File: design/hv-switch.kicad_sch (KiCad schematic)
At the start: 29 parts, among them Q3 GAN080-650EBE, U7 MAX22702EASA+

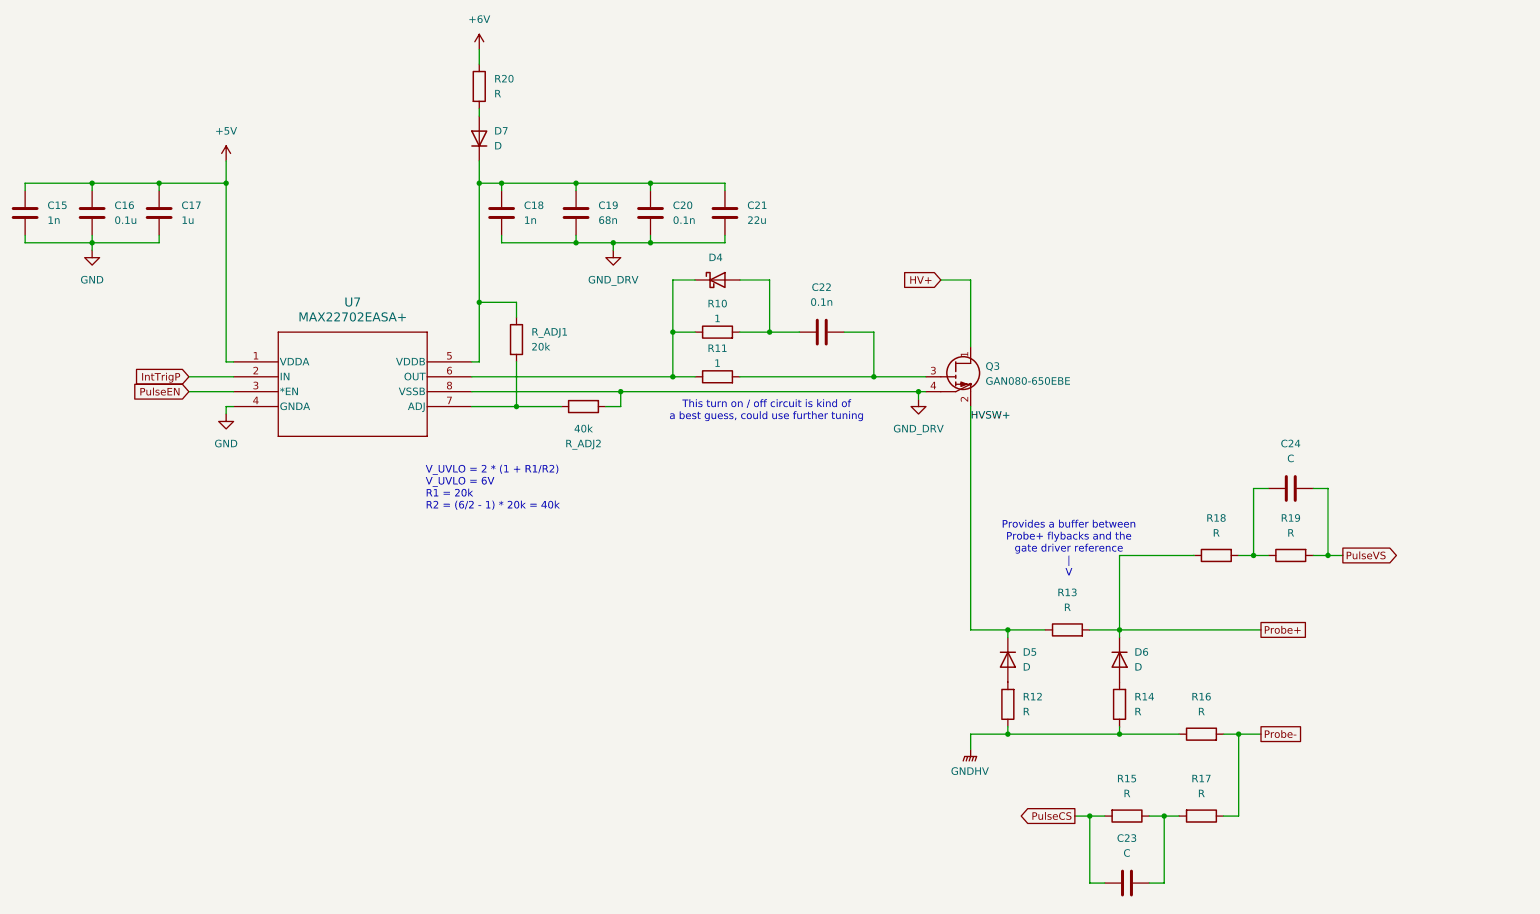
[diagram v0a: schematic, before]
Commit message: working on measurement buffers
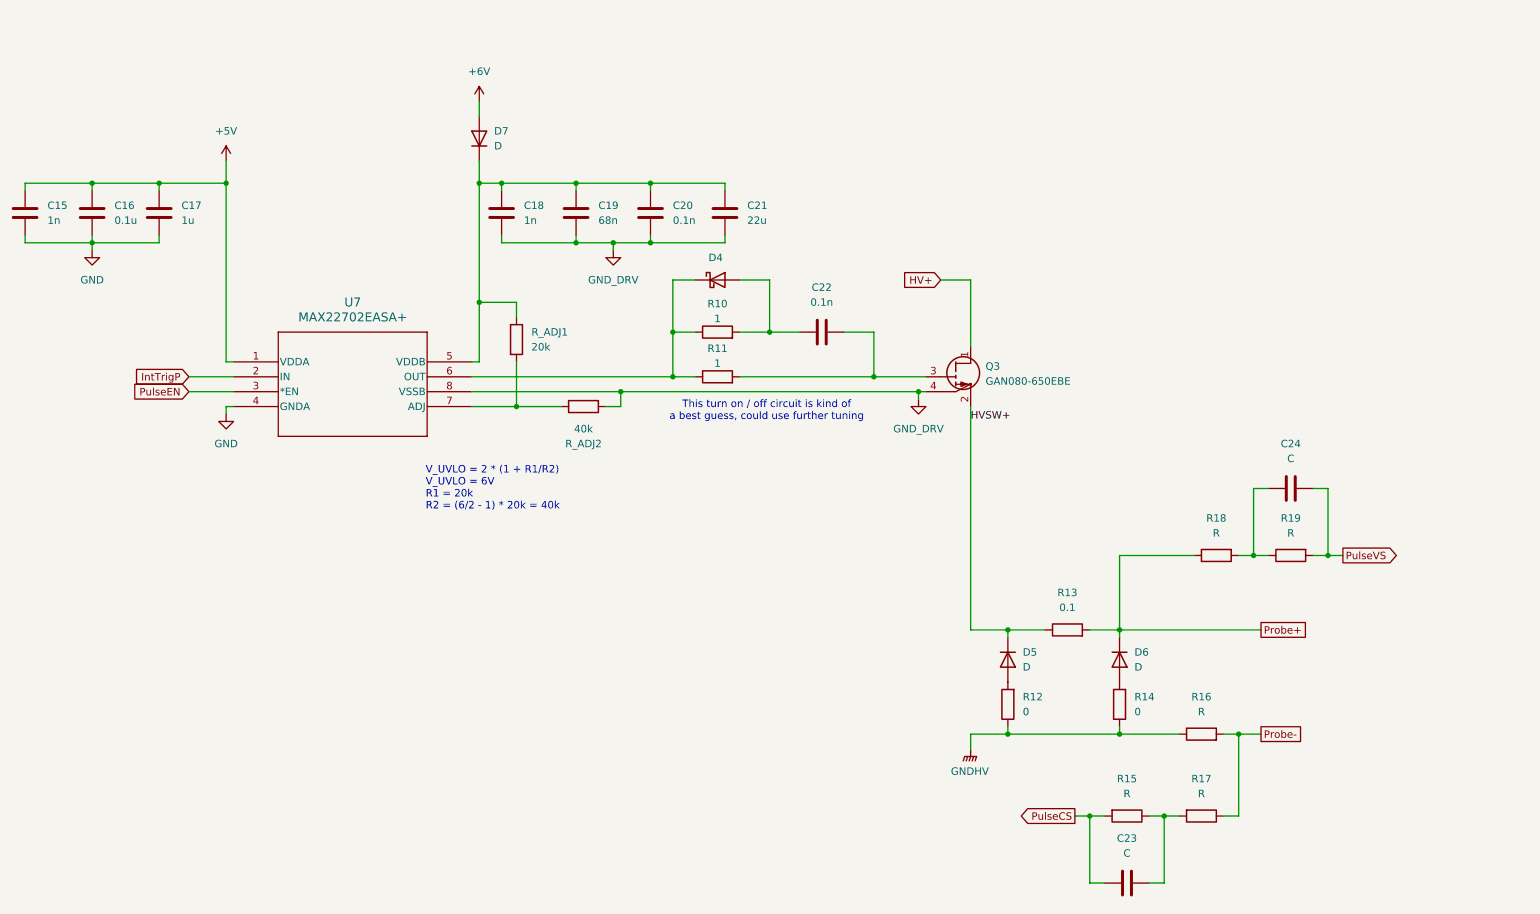
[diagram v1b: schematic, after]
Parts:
- removed R20: R, symbol Device:R
- R12, R14: value R -> 0
- R13: value R -> 0.1
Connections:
- net +6V: now also D7.2 (A)
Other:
- note removed: "Provides a buffer between Probe+ flybacks and the gate driver reference | V"
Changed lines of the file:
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@@
 		)
 	)
-	(text "Provides a buffer between \nProbe+ flybacks and the \ngate driver reference\n|\nV"
-		(exclude_from_sim no)
-		(at 212.344 105.664 0)
-		(effects
-			(font
-				(size 1.27 1.27)
-			)
-		)
-	)
 	(junction
 		(at 243.84 106.68)
@@
 	(wire
 		(pts
+			(xy 111.76 29.21) (xy 111.76 31.75)
+		)
+		(stroke
+			(width 0)
+			(type default)
+		)
+	)
+	(wire
+		(pts
 			(xy 213.36 151.13) (xy 215.9 151.13)
 		)
@@
 	(wire
 		(pts
-			(xy 111.76 30.48) (xy 111.76 31.75)
-		)
-		(stroke
-			(width 0)
-			(type default)
-		)
-	)
-	(wire
-		(pts
 			(xy 118.11 63.5) (xy 111.76 63.5)
 		)
@@
 	(wire
 		(pts
-			(xy 111.76 20.32) (xy 111.76 22.86)
-		)
-		(stroke
-			(width 0)
-			(type default)
-		)
-	)
-	(wire
-		(pts
 			(xy 241.3 151.13) (xy 238.76 151.13)
 		)
@@
 	(symbol
 		(lib_id "power:VDD")
-		(at 111.76 20.32 0)
+		(at 111.76 29.21 0)
 		(unit 1)
 		(exclude_from_sim no)
@@
 		(fields_autoplaced yes)
 		(property "Reference" "#PWR034"
-			(at 111.76 24.13 0)
+			(at 111.76 33.02 0)
 			(effects
 				(font
@@
 		)
 		(property "Value" "+6V"
-			(at 111.76 15.24 0)
+			(at 111.76 24.13 0)
 			(effects
 				(font
@@
 		)
 		(property "Footprint" ""
-			(at 111.76 20.32 0)
+			(at 111.76 29.21 0)
 			(effects
 				(font
@@
 		)
 		(property "Datasheet" ""
-			(at 111.76 20.32 0)
+			(at 111.76 29.21 0)
 			(effects
 				(font
@@
 		)
 		(property "Description" "Power symbol creates a global label with name \"VDD\""
-			(at 111.76 20.32 0)
+			(at 111.76 29.21 0)
 			(effects
 				(font
@@
 	)
 	(symbol
-		(lib_id "Device:R")
-		(at 111.76 26.67 0)
-		(unit 1)
-		(exclude_from_sim no)
-		(in_bom yes)
-		(on_board yes)
-		(dnp no)
-		(fields_autoplaced yes)
-		(property "Reference" "R20"
-			(at 114.3 25.3999 0)
-			(effects
-				(font
-					(size 1.27 1.27)
-				)
-				(justify left)
-			)
-		)
-		(property "Value" "R"
-			(at 114.3 27.9399 0)
-			(effects
-				(font
-					(size 1.27 1.27)
-				)
-				(justify left)
-			)
-		)
-		(property "Footprint" ""
-			(at 109.982 26.67 90)
-			(effects
-				(font
-					(size 1.27 1.27)
-				)
-				(hide yes)
-			)
-		)
-		(property "Datasheet" "~"
-			(at 111.76 26.67 0)
-			(effects
-				(font
-					(size 1.27 1.27)
-				)
-				(hide yes)
-			)
-		)
-		(property "Description" "Resistor"
-			(at 111.76 26.67 0)
-			(effects
-				(font
-					(size 1.27 1.27)
-				)
-				(hide yes)
-			)
-		)
-		(pin "2"
-		)
-		(pin "1"
-		)
-		(instances
-			(project ""
-				(path "/e1be550d-9ce6-42b1-a89a-c00b9d7586dd/a0344160-5a1e-4ade-9868-d857907b9d6d"
-					(reference "R20")
-					(unit 1)
-				)
-			)
-		)
-	)
-	(symbol
 		(lib_id "power:VDD")
 		(at 68.58 39.37 0)
@@
 			)
 		)
-		(property "Value" "R"
+		(property "Value" "0"
 			(at 204.47 133.3499 0)
 			(effects
@@
 			)
 		)
-		(property "Value" "R"
+		(property "Value" "0.1"
 			(at 212.09 115.57 90)
 			(effects
@@
 			)
 		)
-		(property "Value" "R"
+		(property "Value" "0"
 			(at 223.52 133.3499 0)
 			(effects

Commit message: Working on measure buffers and assigning footprints
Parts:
- added C9: 10p, Capacitor_SMD:C_0402_1005Metric, symbol Device:C
- added R20, R4: 4.7M, symbol Device:R
- added R3: 4.3M, symbol Device:R
- C15, C16, C17, C18, C19, C20, C21, C22: footprint (none) -> Capacitor_SMD:C_0402_1005Metric
- C23, C24: value C -> 10p; footprint (none) -> Capacitor_SMD:C_0402_1005Metric
- R15: value R -> 4.3M
- R16: value R -> 0.02
- R17, R18: value R -> 330
- R19: value R -> 10M
- R_ADJ1, R_ADJ2: footprint (none) -> Resistor_SMD:R_0402_1005Metric
- U7: footprint 21-0041-A_8L -> project-footprints:21-0041-A_8L
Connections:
- net PulseCS: now also R15.1; no longer R15.2
- net PulseVS: now also C9.1, R4.2; no longer C24.1, R19.2
- net at C23.2, R17.2: now also R20.2; no longer R15.1
- new net: R3.2, R4.1
- new net: R19.2, R3.1
- new net: R15.2, R20.1
- new net: C24.1, C9.2
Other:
- note added: "10:1 Attenuator"
- note added: "20:1 Attenuator"
- moved on the sheet: C23, R18, R19

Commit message: _
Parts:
- added R24, R25, R26, R27, R28: 20m, Resistor_SMD:R_0805_2012Metric, symbol Device:R
- R10, R11: footprint (none) -> Resistor_SMD:R_0603_1608Metric
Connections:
- new net: R27.1, R28.1
- new net: R25.1, R26.1
- new net: R26.2, R27.2
- new net: R24.2, R25.2

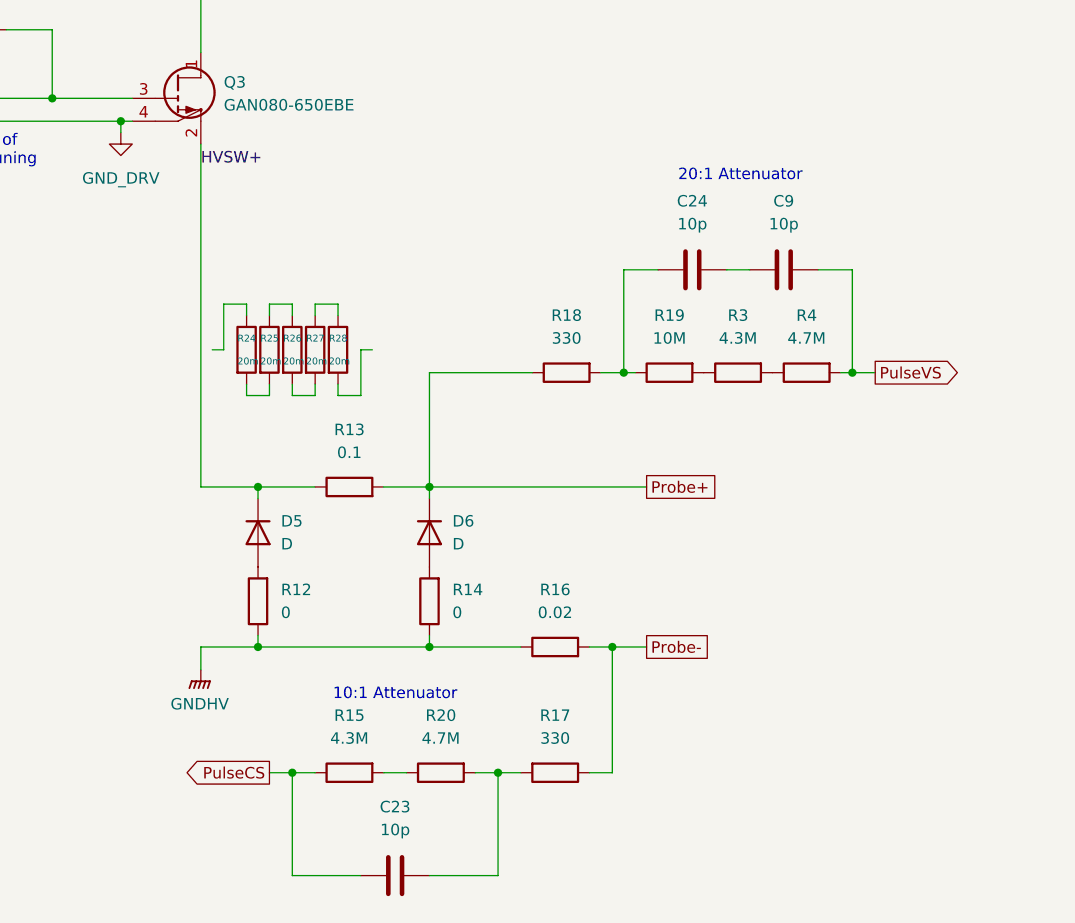
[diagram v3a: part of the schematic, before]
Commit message: Added resistor networks
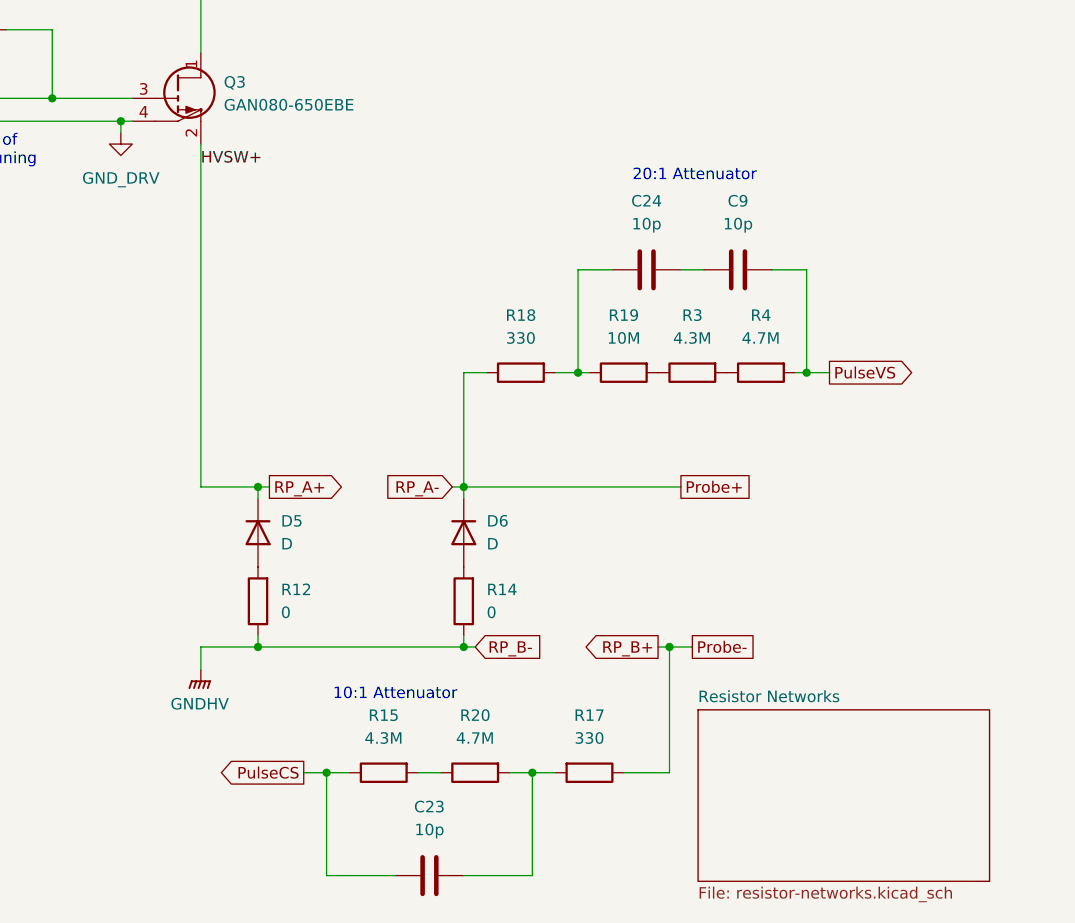
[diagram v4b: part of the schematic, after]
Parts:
- removed R13: 0.1, symbol Device:R
- removed R16: 0.02, symbol Device:R
- removed R24, R25, R26, R27, R28: 20m, Resistor_SMD:R_0805_2012Metric, symbol Device:R
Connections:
- net HVSW+ renamed RP_A+
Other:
- added sheet Resistor Networks (resistor-networks.kicad_sch)
- moved on the sheet: C23, C24, C9, D6, R14, R15, R17, R18, R19, R20, R3, R4

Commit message: more footprint assignment
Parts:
- D4: footprint (none) -> Diode_SMD:D_SOD-123
- D5, D6: value D -> HF1600G; footprint (none) -> Diode_THT:D_DO-41_SOD81_P7.62mm_Horizontal
- R12, R14: value 0 -> 0R, 200V, 30A; footprint (none) -> Resistor_SMD:R_2512_6332Metric
- R15, R17, R18, R19, R20: footprint (none) -> Resistor_SMD:R_0603_1608Metric
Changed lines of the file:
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@@
 			)
 		)
-		(property "Footprint" ""
+		(property "Footprint" "Resistor_SMD:R_0603_1608Metric"
 			(at 242.57 104.902 90)
 			(effects
@@
 			)
 		)
-		(property "Value" "D"
+		(property "Value" "HF1600G"
 			(at 204.47 125.7299 90)
 			(effects
@@
 			)
 		)
-		(property "Footprint" ""
+		(property "Footprint" "Diode_THT:D_DO-41_SOD81_P7.62mm_Horizontal"
 			(at 201.93 124.46 0)
 			(effects
@@
 			)
 		)
-		(property "Footprint" ""
+		(property "Footprint" "Resistor_SMD:R_0603_1608Metric"
 			(at 215.9 149.352 90)
 			(effects
@@
 			)
 		)
-		(property "Footprint" ""
+		(property "Footprint" "Diode_SMD:D_SOD-123"
 			(at 152.4 59.69 0)
 			(effects
@@
 			)
 		)
-		(property "Footprint" ""
+		(property "Footprint" "Resistor_SMD:R_0603_1608Metric"
 			(at 238.76 149.352 90)
 			(effects
@@
 			)
 		)
-		(property "Footprint" ""
+		(property "Footprint" "Resistor_SMD:R_0603_1608Metric"
 			(at 231.14 104.902 90)
 			(effects
@@
 			)
 		)
-		(property "Value" "0"
+		(property "Value" "0R, 200V, 30A"
 			(at 204.47 133.3499 0)
 			(effects
@@
 			)
 		)
-		(property "Footprint" ""
+		(property "Footprint" "Resistor_SMD:R_2512_6332Metric"
 			(at 203.708 132.08 90)
 			(effects
@@
 			)
 		)
-		(property "Description" "Resistor"
+		(property "Description" "HoT2512D-3W-0R"
 			(at 201.93 132.08 0)
 			(effects
@@
 			)
 		)
-		(property "Value" "D"
+		(property "Value" "HF1600G"
 			(at 227.33 125.7299 90)
 			(effects
@@
 			)
 		)
-		(property "Footprint" ""
+		(property "Footprint" "Diode_THT:D_DO-41_SOD81_P7.62mm_Horizontal"
 			(at 224.79 124.46 0)
 			(effects
@@
 			)
 		)
-		(property "Value" "0"
+		(property "Value" "0R, 200V, 30A"
 			(at 227.33 133.3499 0)
 			(effects
@@
 			)
 		)
-		(property "Footprint" ""
+		(property "Footprint" "Resistor_SMD:R_2512_6332Metric"
 			(at 226.568 132.08 90)
 			(effects
@@
 			)
 		)
-		(property "Description" "Resistor"
+		(property "Description" "HoT2512D-3W-0R"
 			(at 224.79 132.08 0)
 			(effects
@@
 			)
 		)
-		(property "Footprint" ""
+		(property "Footprint" "Resistor_SMD:R_0603_1608Metric"
 			(at 226.06 149.352 90)
 			(effects

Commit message: Footprint assignment / part selection
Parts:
- renumbered C15 to C24, C16 to C25, C17 to C26, C18 to C27, C19 to C28, C20 to C29, C21 to C30, C22 to C31, C24 to C32, C9 to C33, C23 to C34, D7 to D6, D4 to D7, D5 to D8, D6 to D9, R10 to R15, R11 to R16, R18 to R17, R19 to R18, R3 to R19, R4 to R20, R12 to R21, R14 to R22, R15 to R23, R20 to R24, R17 to R25, U7 to U9

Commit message: More footprint assignment and component selection
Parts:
- R19: footprint (none) -> Resistor_SMD:R_0603_1608Metric
- R20: footprint (none) -> Resistor_SMD:R_2512_6332Metric
- R23, R24, R25: footprint Resistor_SMD:R_0603_1608Metric -> Resistor_SMD:R_2512_6332Metric
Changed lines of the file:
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@@
 			)
 		)
-		(property "Footprint" ""
+		(property "Footprint" "Resistor_SMD:R_2512_6332Metric"
 			(at 257.81 104.902 90)
 			(effects
@@
 			)
 		)
-		(property "Footprint" ""
+		(property "Footprint" "Resistor_SMD:R_0603_1608Metric"
 			(at 250.19 104.902 90)
 			(effects
@@
 			)
 		)
-		(property "Footprint" "Resistor_SMD:R_0603_1608Metric"
+		(property "Footprint" "Resistor_SMD:R_2512_6332Metric"
 			(at 215.9 149.352 90)
 			(effects
@@
 			)
 		)
-		(property "Footprint" "Resistor_SMD:R_0603_1608Metric"
+		(property "Footprint" "Resistor_SMD:R_2512_6332Metric"
 			(at 238.76 149.352 90)
 			(effects
@@
 			)
 		)
-		(property "Footprint" "Resistor_SMD:R_0603_1608Metric"
+		(property "Footprint" "Resistor_SMD:R_2512_6332Metric"
 			(at 226.06 149.352 90)
 			(effects

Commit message: More footprint assignment (almost done)
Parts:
- Q3: footprint (none) -> project-footprints:GAN080650EBEZ
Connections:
- net PulseVS renamed PulseVS+
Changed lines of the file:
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@@
+	(wire
+		(pts
+			(xy 262.89 110.49) (xy 265.43 110.49)
+		)
+		(stroke
+			(width 0)
+			(type default)
+		)
+	)
 	(wire
 		(pts
@@
 		(pts
 			(xy 190.5 59.69) (xy 195.58 59.69)
+		)
+		(stroke
+			(width 0)
+			(type default)
+		)
+	)
+	(wire
+		(pts
+			(xy 262.89 113.03) (xy 262.89 110.49)
 		)
 		(stroke
@@
 		)
 	)
-	(global_label "PulseVS"
+	(global_label "PulseVS+"
 		(shape output)
 		(at 265.43 106.68 0)
@@
 		)
 		(property "Intersheetrefs" "${INTERSHEET_REFS}"
-			(at 279.1799 106.68 0)
+			(at 277.4866 106.68 0)
+			(effects
+				(font
+					(size 1.27 1.27)
+				)
+				(justify left)
+				(hide yes)
+			)
+		)
+	)
+	(global_label "PulseVS-"
+		(shape output)
+		(at 265.43 110.49 0)
+		(fields_autoplaced yes)
+		(effects
+			(font
+				(size 1.27 1.27)
+			)
+			(justify left)
+		)
+		(property "Intersheetrefs" "${INTERSHEET_REFS}"
+			(at 277.4866 110.49 0)
 			(effects
 				(font
@@
 	)
 	(symbol
+		(lib_id "power:GNDPWR")
+		(at 262.89 113.03 0)
+		(unit 1)
+		(exclude_from_sim no)
+		(in_bom yes)
+		(on_board yes)
+		(dnp no)
+		(fields_autoplaced yes)
+		(property "Reference" "#PWR043"
+			(at 262.89 118.11 0)
+			(effects
+				(font
+					(size 1.27 1.27)
+				)
+				(hide yes)
+			)
+		)
+		(property "Value" "GNDHV"
+			(at 262.763 116.84 0)
+			(effects
+				(font
+					(size 1.27 1.27)
+				)
+			)
+		)
+		(property "Footprint" ""
+			(at 262.89 114.3 0)
+			(effects
+				(font
+					(size 1.27 1.27)
+				)
+				(hide yes)
+			)
+		)
+		(property "Datasheet" ""
+			(at 262.89 114.3 0)
+			(effects
+				(font
+					(size 1.27 1.27)
+				)
+				(hide yes)
+			)
+		)
+		(property "Description" "Power symbol creates a global label with name \"GNDPWR\" , global ground"
+			(at 262.89 113.03 0)
+			(effects
+				(font
+					(size 1.27 1.27)
+				)
+				(hide yes)
+			)
+		)
+		(pin "1"
+		)
+		(instances
+			(project "BitCrusher"
+				(path "/e1be550d-9ce6-42b1-a89a-c00b9d7586dd/a0344160-5a1e-4ade-9868-d857907b9d6d"
+					(reference "#PWR043")
+					(unit 1)
+				)
+			)
+		)
+	)
+	(symbol
 		(lib_id "Device:C")
 		(at 153.67 48.26 0)
@@
 			)
 		)
-		(property "Footprint" ""
+		(property "Footprint" "project-footprints:GAN080650EBEZ"
 			(at 198.12 78.105 0)
 			(effects
